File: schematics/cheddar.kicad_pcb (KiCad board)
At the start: 2 copper layers, 43 x 26 mm, 31 parts, among them J1 BATT_CONN, J2 EXTERNAL_TRIGGER, J3 USB_OTG, J4 Conn_01x08, J5 Conn_01x08, Q1 MOSFET_PCH, SW1 SW_Push, U1 ESP-12E, U2 ch340g, U3 MCP73831, U4 HT7333, Y1 12Mhz

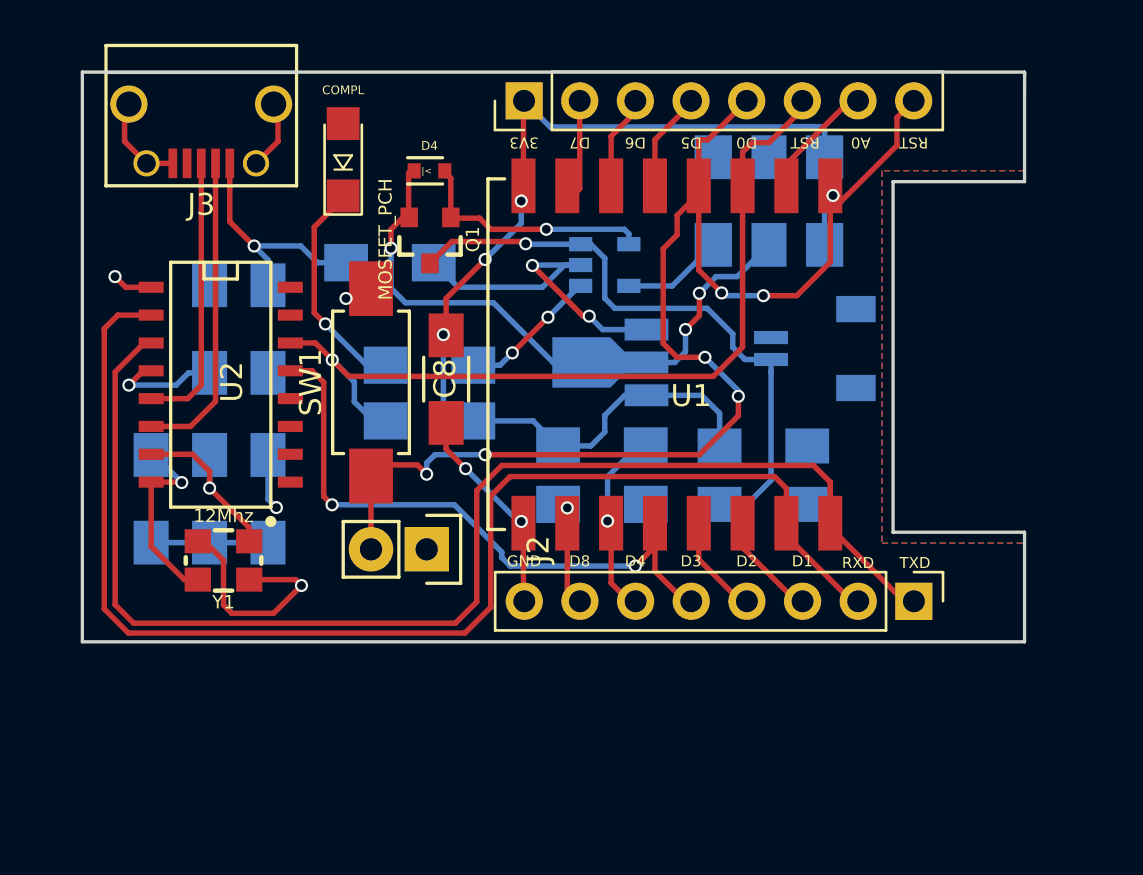
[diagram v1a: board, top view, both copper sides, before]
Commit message: replace all footprints with standard lib ones
remove unnecessary custom libs
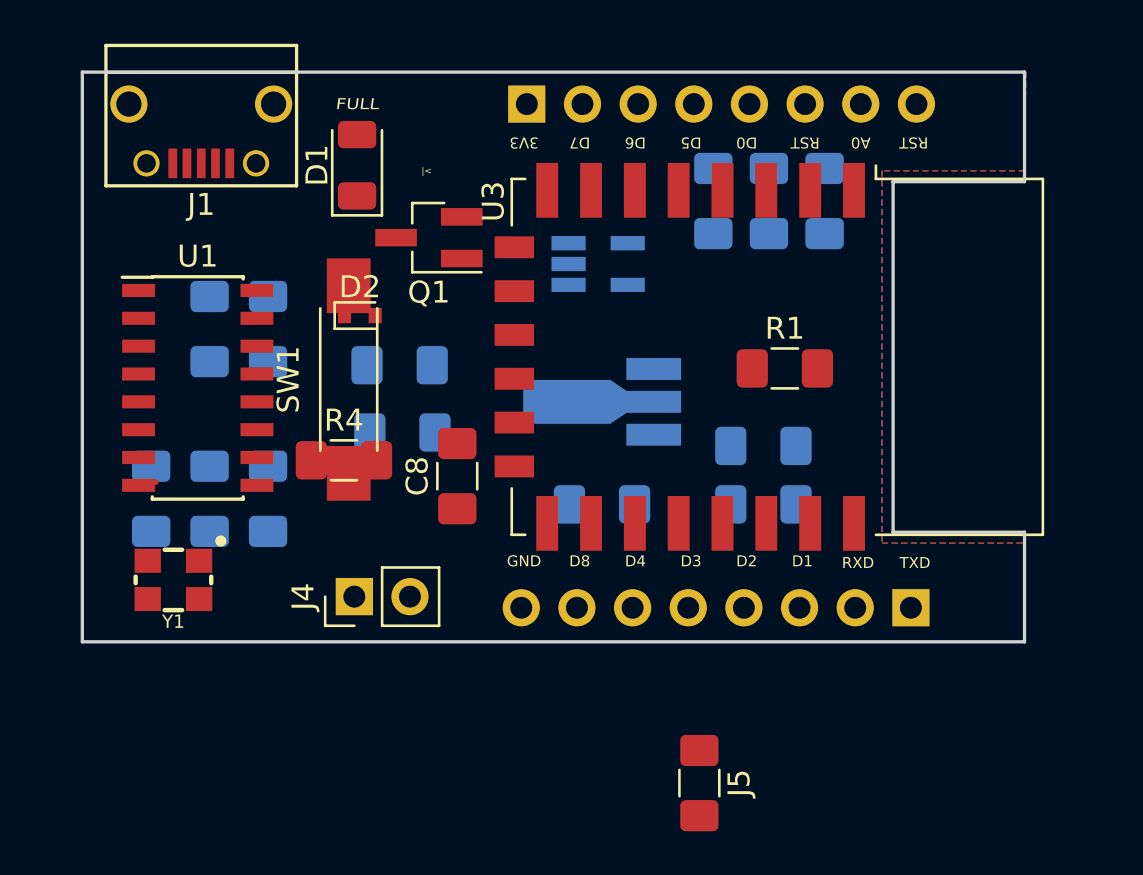
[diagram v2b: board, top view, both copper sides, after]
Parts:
- removed D4: D_Schottky, Diodes_SMD:SOD-523
- removed R8: 10k, Resistors_SMD:R_1206_HandSoldering
- removed R9: 100k, Resistors_SMD:R_1206_HandSoldering
- removed URLAB-LOGO1: logo, custom-cheddar:urlab
- added D2: D_Schottky, Diode_SMD:D_SOD-523, F.Cu at (145.0, 101.5)
- added R1: 10k, Resistor_SMD:R_1206_3216Metric_Pad1.42x1.75mm_HandSolder, F.Cu at (164.4, 103.9)
- added R4: 100k, Resistor_SMD:R_1206_3216Metric_Pad1.42x1.75mm_HandSolder, F.Cu at (144.3, 108.1)
- C1: value 220uF -> 100nF; footprint Capacitors_SMD:C_1206_HandSoldering -> Capacitor_SMD:C_1206_3216Metric_Pad1.42x1.75mm_HandSolder
- C2: value 22pF -> 10nF; footprint Capacitors_SMD:C_1206_HandSoldering -> Capacitor_SMD:C_1206_3216Metric_Pad1.42x1.75mm_HandSolder
- C3: value 22pF -> 22nF; footprint Capacitors_SMD:C_1206_HandSoldering -> Capacitor_SMD:C_1206_3216Metric_Pad1.42x1.75mm_HandSolder
- C4: value 100nF -> 22pF; footprint Capacitors_SMD:C_1206_HandSoldering -> Capacitor_SMD:C_1206_3216Metric_Pad1.42x1.75mm_HandSolder
- C5: value 10nF -> 22pF; footprint Capacitors_SMD:C_1206_HandSoldering -> Capacitor_SMD:C_1206_3216Metric_Pad1.42x1.75mm_HandSolder
- C6: value 22nF -> 100nF; footprint Capacitors_SMD:C_1206_HandSoldering -> Capacitor_SMD:C_1206_3216Metric_Pad1.42x1.75mm_HandSolder
- C7, C9: footprint Capacitors_SMD:C_1206_HandSoldering -> Capacitor_SMD:C_1206_3216Metric_Pad1.42x1.75mm_HandSolder
- C8: value 100nF -> 220uF; footprint Capacitors_SMD:C_1206_HandSoldering -> Capacitor_SMD:C_1206_3216Metric_Pad1.42x1.75mm_HandSolder
- D1: footprint LEDs:LED_1206 -> LED_SMD:LED_1206_3216Metric
- J1: value BATT_CONN -> USB_OTG; footprint Connectors_JST:JST_SH_SM02B-SRSS-TB_02x1.00mm_Angled -> custom-cheddar:USB_Micro-B-custom; moved to F.Cu
- J2: value EXTERNAL_TRIGGER -> Conn_01x08; footprint Pin_Headers:Pin_Header_Straight_1x02 -> Connector_PinHeader_2.54mm:PinHeader_1x08_P2.54mm_Vertical; moved to B.Cu
- J3: value USB_OTG -> Conn_01x08; footprint custom-cheddar:USB_Micro-B-custom -> Connector_PinHeader_2.54mm:PinHeader_1x08_P2.54mm_Vertical; moved to B.Cu
- J4: value Conn_01x08 -> EXTERNAL_TRIGGER; footprint Pin_Headers:Pin_Header_Straight_1x08_Pitch2.54mm -> Connector_PinHeader_2.54mm:PinHeader_1x02_P2.54mm_Vertical
- J5: value Conn_01x08 -> BATT_CONN; footprint Pin_Headers:Pin_Header_Straight_1x08_Pitch2.54mm -> Resistor_SMD:R_1206_3216Metric_Pad1.42x1.75mm_HandSolder
- Q1: footprint Silicon-Standard:SOT23-3 -> Package_TO_SOT_SMD:SOT-23_Handsoldering
- R2: value 470 -> 10k; footprint Resistors_SMD:R_1206_HandSoldering -> Resistor_SMD:R_1206_3216Metric_Pad1.42x1.75mm_HandSolder
- R3: value 10k -> 470; footprint Resistors_SMD:R_1206_HandSoldering -> Resistor_SMD:R_1206_3216Metric_Pad1.42x1.75mm_HandSolder
- R5, R6, R7: footprint Resistors_SMD:R_1206_HandSoldering -> Resistor_SMD:R_1206_3216Metric_Pad1.42x1.75mm_HandSolder
- SW1: footprint Buttons_Switches_SMD:SW_SPST_REED_CT05-XXXX-G1 -> Button_Switch_SMD:SW_SPST_REED_CT05-XXXX-G1
- U1: value ESP-12E -> CH340G; footprint ESP8266:ESP-12E_SMD -> Package_SO:SOIC-16_3.9x9.9mm_P1.27mm
- U2: value ch340g -> MCP73831; footprint SMD_Packages:SO-16-N -> Package_TO_SOT_SMD:SOT-23-5_HandSoldering; moved to B.Cu
- U3: value MCP73831 -> ESP-12E; footprint sot:SOT23-5 -> RF_Module:ESP-12E; moved to F.Cu
- U4: footprint sot:SOT89 -> Package_TO_SOT_SMD:SOT-89-3_Handsoldering
- Y1: footprint Clocks:CRYSTAL-SMD-3.2X2.5MM -> custom-cheddar:CRYSTAL-SMD-3.2X2.5MM
- moved J3 39.1 mm to (170.2, 114.8), turned to 90 degrees
- moved U1 30.1 mm to (137.6, 104.8), turned to 0 degrees
- moved J1 29.7 mm to (137.8, 93.0), turned to 180 degrees
- moved J4 23.9 mm to (144.8, 114.3)
- moved J2 20.8 mm to (152.7, 91.8)
- moved U2 18.1 mm to (155.9, 99.1), turned to 0 degrees
- moved J5 12.8 mm to (160.5, 122.8)
- moved U3 8.92 mm to (164.1, 103.4), turned to 270 degrees
- moved C8 4.46 mm to (149.5, 108.8)
- moved Y1 2.45 mm to (136.5, 113.5)
- moved U4 1.80 mm to (156.5, 105.4)
- moved R2 1.36 mm to (146.8, 103.7)
- moved R6 1.34 mm to (147.0, 106.8)
- moved SW1 1.02 mm to (144.5, 104.4)
- moved D1 0.68 mm to (144.9, 94.6)
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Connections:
- C1 pad 1: Net-(C1-Pad1) -> GND
- C1 pad 2: GND -> +5V
- C2 pad 1: /XI -> GND
- C2 pad 2: GND -> +5V
- C3 pad 1: /XO -> Net-(C3-Pad1)
- C4 pad 1: GND -> /XI
- C4 pad 2: +5V -> GND
- C5 pad 1: GND -> /XO
- C5 pad 2: +5V -> GND
- C6 pad 1: Net-(C6-Pad1) -> GND
- C6 pad 2: GND -> +3V3
- C8 pad 1: GND -> Net-(C8-Pad1)
- C8 pad 2: +3V3 -> GND
- J1 pad 1: GND -> +5V
- J1 pad 2: Net-(C7-Pad2) -> /D-
- J2 pad 1: GND -> +3V3
- J2 pad 2: /GPIO16 -> /GPIO13
- J3 pad 1: +5V -> /TXD
- J3 pad 2: /D- -> /RXD
- J3 pad 3: /D+ -> /GPIO5
- J3 pad 4: (no net) -> /GPIO4
- J3 pad 5: GND -> /GPIO0
- J3 pad 6: GND -> /GPIO2
- J4 pad 1: +3V3 -> GND
- J4 pad 2: /GPIO13 -> /GPIO16
- J5 pad 1: /TXD -> GND
- J5 pad 2: /RXD -> Net-(C7-Pad2)
- Q1 pad 2: Net-(C1-Pad1) -> Net-(C7-Pad2)
- Q1 pad 3: Net-(C7-Pad2) -> Net-(C8-Pad1)
- R2 pad 1: Net-(R2-Pad1) -> +3V3
- R2 pad 2: Net-(D1-Pad1) -> /GPIO16
- R3 pad 1: GND -> Net-(R3-Pad1)
- R3 pad 2: Net-(R3-Pad2) -> Net-(D1-Pad1)
- R5 pad 1: +3V3 -> /GPIO15
- R5 pad 2: /GPIO16 -> GND
- R7 pad 1: /GPIO15 -> /GPIO2
- R7 pad 2: GND -> +3V3
- U1 pad 1: /GPIO16 -> GND
- U1 pad 10: /GPIO15 -> (no net)
- U1 pad 11: /GPIO2 -> (no net)
- U1 pad 12: /GPIO0 -> (no net)
- U1 pad 13: /GPIO4 -> /GPIO0
- U1 pad 14: /GPIO5 -> /CH_PD
- U1 pad 15: /RXD -> (no net)
- U1 pad 16: /TXD -> +5V
- U1 pad 2: /ADC -> /TXD
- U1 pad 3: /CH_PD -> /RXD
- U1 pad 4: /GPIO16 -> Net-(C3-Pad1)
- U1 pad 5: /GPIO14 -> /D+
- U1 pad 6: /GPIO12 -> /D-
- U1 pad 7: /GPIO13 -> /XI
- U1 pad 8: +3V3 -> /XO
- U1 pad 9: GND -> (no net)
- U2 pad 1: GND -> Net-(R3-Pad1)
- U2 pad 2: /RXD -> GND
- U2 pad 3: /TXD -> Net-(C7-Pad2)
- U2 pad 4: Net-(C6-Pad1) -> +5V
- U2 pad 5: /D+ -> Net-(R1-Pad1)
- U3 pad 1: Net-(R2-Pad1) -> /GPIO16
- U3 pad 2: GND -> /ADC
- U3 pad 3: Net-(C7-Pad2) -> /CH_PD
- U3 pad 4: +5V -> /GPIO16
- U3 pad 5: Net-(R3-Pad2) -> /GPIO14
- U4 pad 2: Net-(C1-Pad1) -> +3V3
- U4 pad 3: +3V3 -> Net-(C8-Pad1)
- Y1 pad 2: GND -> /XO
- Y1 pad 3: /XO -> (no net)
- Y1 pad 4: GND -> (no net)
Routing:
- net /GPIO16: track 65.9 -> 0.00 mm, vias 7 -> 0
- net /RXD: track 60.5 -> 0.00 mm
- net /TXD: track 60.1 -> 0.00 mm
- net GND: track 55.0 -> 0.00 mm, vias 7 -> 0
- net +3V3: track 49.5 -> 0.00 mm, vias 3 -> 0
- net /CH_PD: track 39.0 -> 0.00 mm, vias 1 -> 0
- net /GPIO0: track 32.5 -> 0.00 mm, vias 2 -> 0
- net Net-(C1-Pad1): track 28.1 -> 0.00 mm, vias 3 -> 0
- net Net-(C7-Pad2): track 28.0 -> 0.00 mm, vias 1 -> 0
- net +5V: track 24.6 -> 0.00 mm, vias 3 -> 0
- net /D-: track 14.3 -> 0.00 mm
- net /D+: track 12.7 -> 0.00 mm
- net /GPIO2: track 10.3 -> 0.00 mm, vias 1 -> 0
- net Net-(D1-Pad1): track 10.1 -> 0.00 mm, vias 1 -> 0
- net /XO: track 9.52 -> 0.24 mm, vias 1 -> 0
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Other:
- board text added: "FULL"
- board text removed: "COMPL"
- board text removed: "tperale & carlos"

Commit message: Reestructure board
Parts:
- J2, J3: moved to F.Cu
- moved J5 20.5 mm to (147.0, 107.5)
- moved R1 15.9 mm to (150.5, 111.5)
- moved D2 9.38 mm to (149.4, 93.2)
- moved R2 8.03 mm to (146.2, 95.7)
- moved R4 6.31 mm to (139.6, 112.3), turned to 270 degrees
- moved C8 5.72 mm to (151.8, 103.6)
- moved R6 4.73 mm to (147.3, 102.1)
- moved U2 3.71 mm to (153.7, 96.2)
- moved C5 3.37 mm to (143.2, 107.4), turned to 270 degrees
- moved Y1 2.90 mm to (134.2, 111.8)
- moved C2 2.84 mm to (139.6, 107.4)
- moved C3 2.51 mm to (136.0, 107.4)
- moved U3 2.51 mm to (166.6, 103.6)
- moved C6 2.48 mm to (136.8, 100.0)
- moved J3 2.45 mm to (172.6, 115.0), turned to 270 degrees
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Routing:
- removed copper zone on F.Cu, net +5V
- removed copper zone on B.Cu, net GND
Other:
- board size 43 x 26 mm -> 47 x 25.9 mm
- board text removed: "|<"
